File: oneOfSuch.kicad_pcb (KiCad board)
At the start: 4 copper layers, 45 x 67 mm, 76 parts, among them J3 I2C_STANDARDQWIIC, J4 Conn_01x13_Pin, J5 USB4520-03-0-A_REVA, J6 I2C_STANDARDQWIIC, J8 Conn_01x13_Pin, U1 ESP32-S3-WROOM-1, U2 AZ1117C, U3 TPS562208

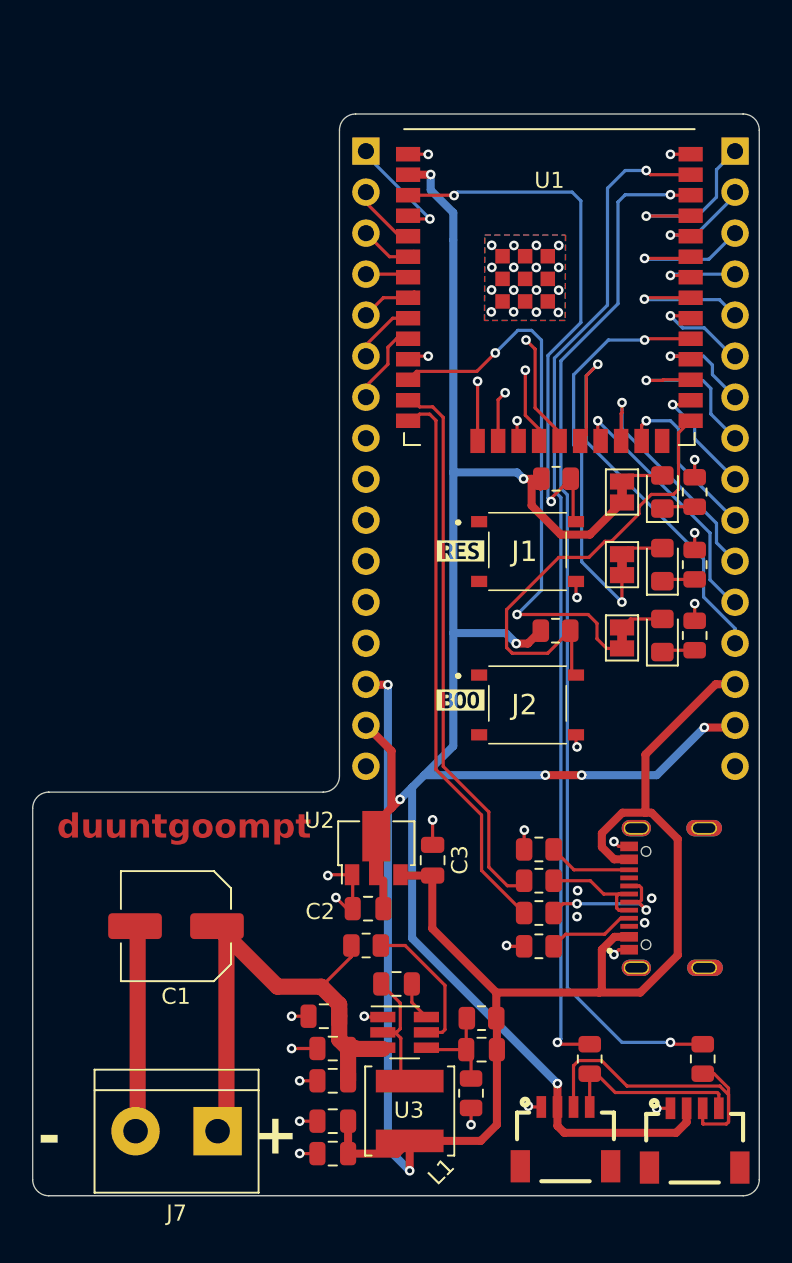
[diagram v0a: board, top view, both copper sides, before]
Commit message: added some stuff to schematic and PCB design
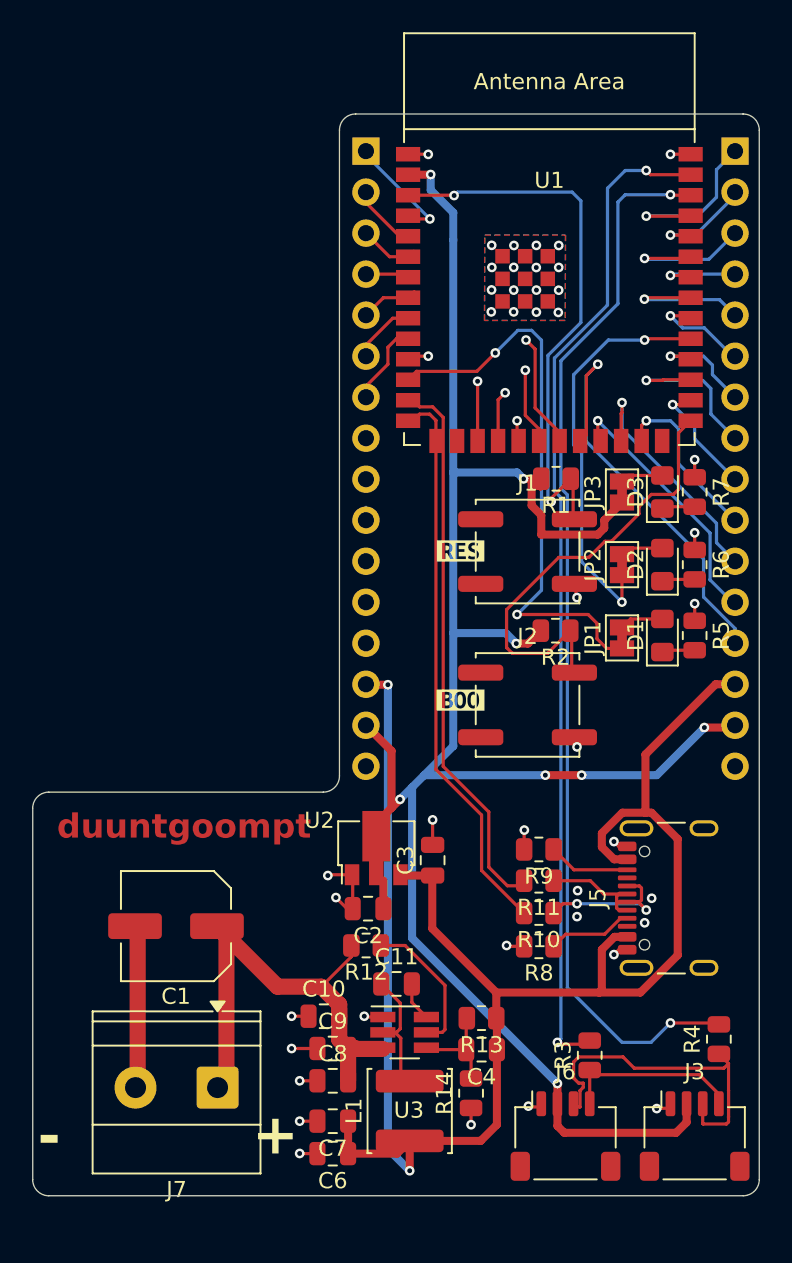
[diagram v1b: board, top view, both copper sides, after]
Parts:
- C10, C11, C2, C3, C4, C6, C7, C8, C9: footprint oneOfSuchFootprints:C_0805_2012Metric -> Capacitor_SMD:C_0805_2012Metric
- D1, D2, D3: footprint oneOfSuchFootprints:LED_0805_2012Metric_Pad1.15x1.40mm_HandSolder -> LED_SMD:LED_0805_2012Metric_Pad1.15x1.40mm_HandSolder
- J1, J2: footprint oneOfSuchFootprints:PTS526SM08SMTR2LFS -> Button_Switch_SMD:SW_Push_1P1T_NO_CK_KSC7xxJ
- J3, J6: footprint oneOfSuchFootprints:1X04_1MM_RA -> Connector_JST:JST_SH_SM04B-SRSS-TB_1x04-1MP_P1.00mm_Horizontal
- J5: footprint oneOfSuchFootprints:GCT_USB4520-03-0-A_REVA -> Connector_USB:USB_C_Receptacle_GCT_USB4105-xx-A_16P_TopMnt_Horizontal
- J7: footprint TerminalBlock:TerminalBlock_bornier-2_P5.08mm -> TerminalBlock_Phoenix:TerminalBlock_Phoenix_MKDS-1,5-2-5.08_1x02_P5.08mm_Horizontal
- JP1, JP2, JP3: footprint oneOfSuchFootprints:SolderJumper-2_P1.3mm_Bridged_Pad1.0x1.5mm -> Jumper:SolderJumper-2_P1.3mm_Bridged_Pad1.0x1.5mm
- L1: footprint oneOfSuchFootprints:L_Changjiang_FNR5020S -> Inductor_SMD:L_Changjiang_FNR5020S
- moved J7 2.70 mm to (130.4, 143.3)
- moved J6 1.80 mm to (152.0, 146.3)
- moved J3 1.72 mm to (160.0, 146.3)
- moved J5 1.59 mm to (159.5, 131.6)
- moved R4 1.58 mm to (161.5, 140.3)
- moved R3 0.23 mm to (153.5, 141.3)
- turned J1 to 180 degrees
- turned J2 to 180 degrees
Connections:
- J1 pad 1: (no net) -> GND
- J2 pad 1: (no net) -> GND
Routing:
- net GND: track 41.2 -> 36.4 mm, vias 43 -> 41
- net +BATT: track 33.3 -> 30.6 mm
- net sda: track 64.8 -> 66.3 mm
- net +5V: track 108.8 -> 109.9 mm, vias 2 -> 3
- net Net-(U1-EN): track 35.1 -> 36.1 mm, vias 2 -> 3
- net +3.3V: track 131.2 -> 132.2 mm
